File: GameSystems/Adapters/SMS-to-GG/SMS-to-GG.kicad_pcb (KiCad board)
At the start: 4 copper layers, 90.6 x 50.4 mm, 5 parts, among them J1 Master System Fingers, J2 Game Gear Slot

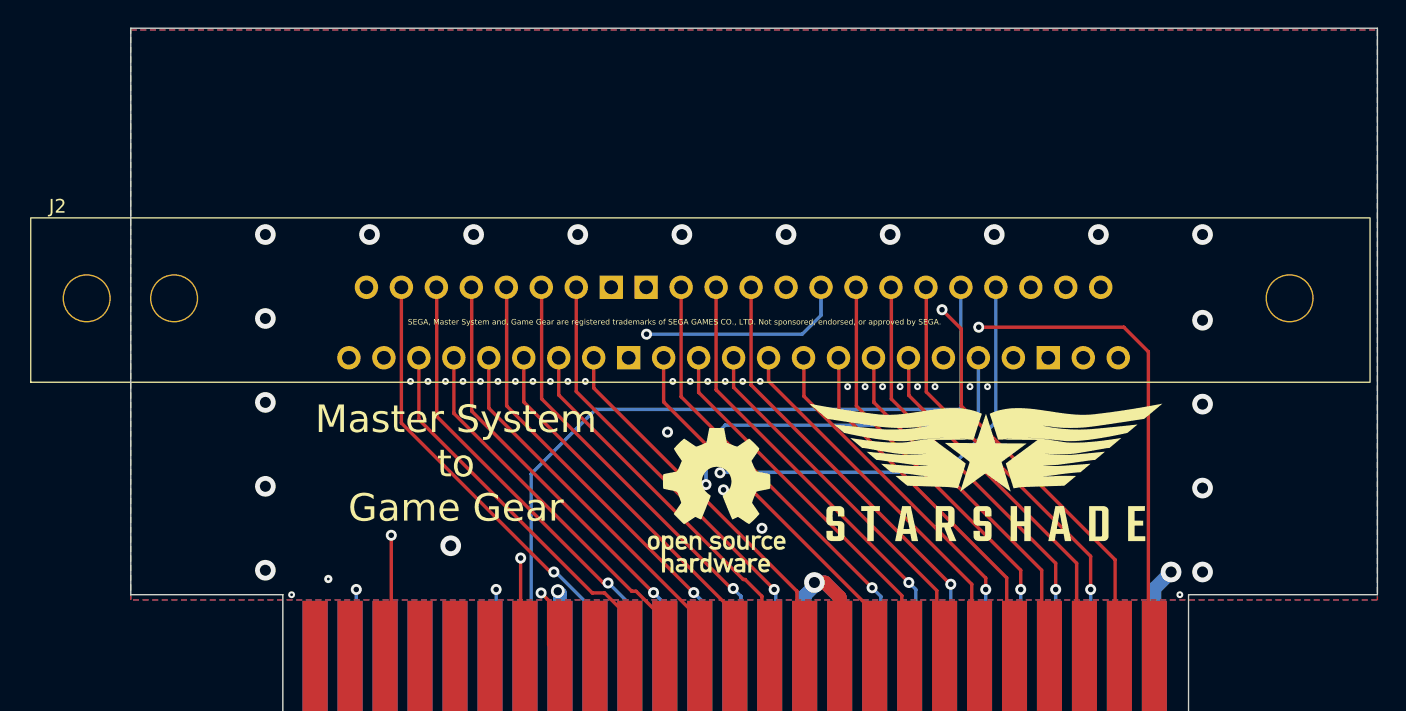
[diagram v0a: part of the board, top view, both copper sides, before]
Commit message: Update SMS to GG adapter and GG slot.
Was electrically correct but the NPTHs were slightly off.
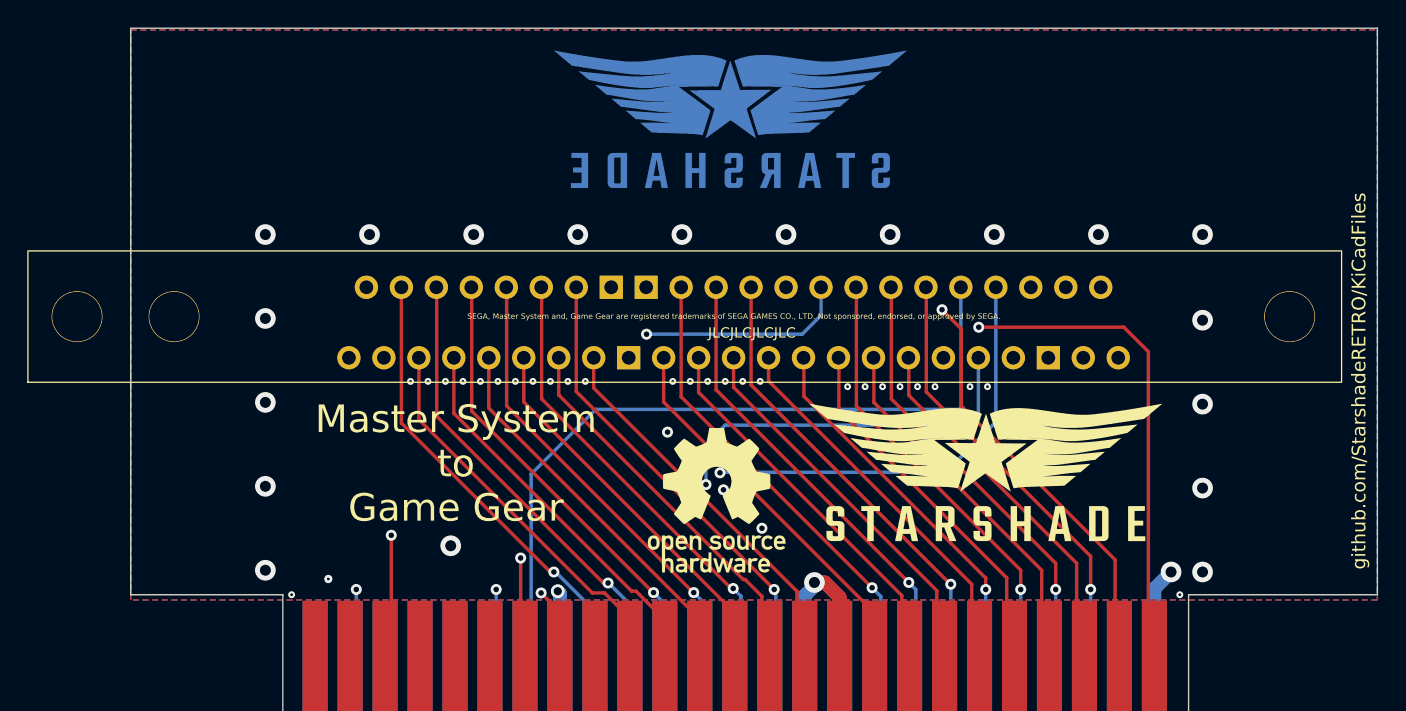
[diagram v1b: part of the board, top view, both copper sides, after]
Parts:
- G***: footprint !MiscFootprints:StarshadeLogoSmall -> !MiscFootprints:StarshadeLogoSmallMask
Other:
- board text added: "JLCJLCJLCJLC"
- board text added: "REV 2"
- board text added: "store.starshade.dev"
- board text removed: "REV 1"

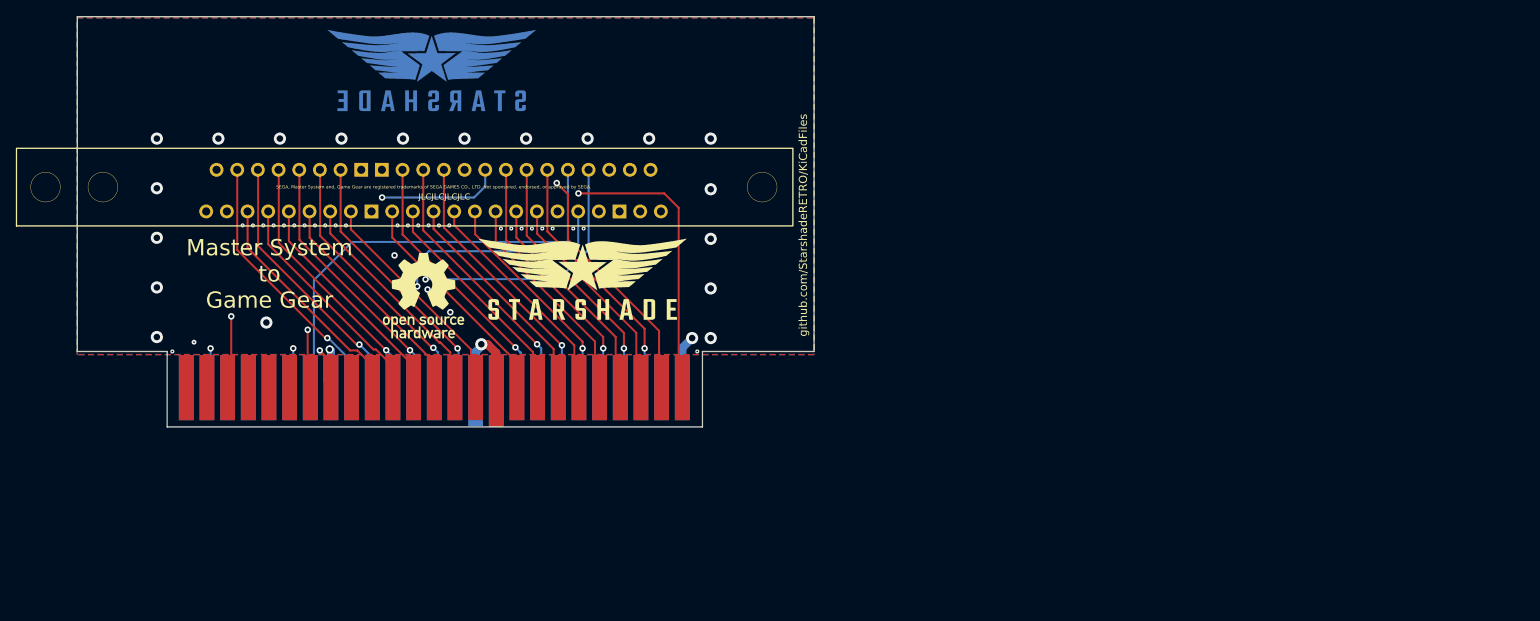
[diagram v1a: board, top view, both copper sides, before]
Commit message: SMS-to-GG revisions + more
* Updated the SMS-to-GG adapter from Rev 2 to Rev 4.
  * Rev 3 (not in repository):
    * Moved GG slot footprint up to allow room for the RetroSix GG slot connector PCB.
    * Added RetroSix GG slot FPC header directly to PCB.
  * Rev 4:
    * Fixed silkscreen disclaimers to refer to SEGA (Japan).
    * Moved JLCPCB "Specify Location" text to under the FPC header.
    * Made some general cosmetic improvements.
    * Updated project files to Latest KiCad version.
* Reorganized the libraries a little.
* Added 2-hole version of the Game Gear slot.
* Updated `.gitignore` for new KiCad version and some plugins.
* Updated the disclaimers in the `README.md` files.
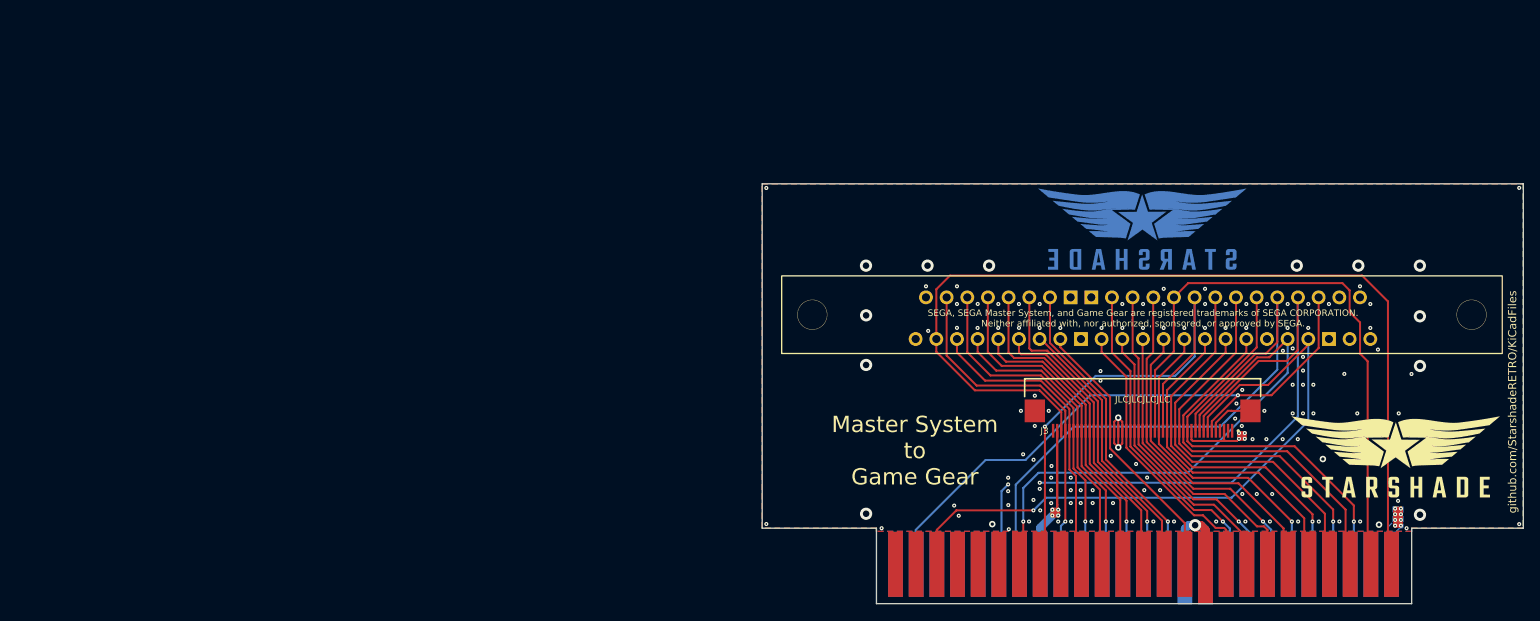
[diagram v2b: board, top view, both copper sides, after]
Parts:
- added J3: Gameslot GG Connector, !MiscFootprints:FPC Connector - 45-pin - Multiple, F.Cu at (150.6, 117.6)
- G***: footprint !MiscFootprints:StarshadeLogoSmall -> !MiscFootprints:Graphic - Starshade Logo - Silk - Small
- G***: footprint !MiscFootprints:OSHW -> !MiscFootprints:Graphic - OSHW Logo - Silk - Small; moved to B.Cu
- G***: footprint !MiscFootprints:StarshadeLogoSmallMask -> !MiscFootprints:Graphic - Starshade Logo - Mask - Small
- J1: value Master System Fingers -> SMS Fingers
- J2: footprint !SGFootprints:SG_GG_CARTRIDGE_SLOT -> !SGFootprints:SG_GG_CARTRIDGE_SLOT_2H
- moved G*** 102.3 mm to (181.7, 120.8)
- moved G*** 91.0 mm to (150.6, 122.7), turned to 180 degrees
- moved J1 89.8 mm to (150.7, 134.0)
- moved G*** 89.5 mm to (150.6, 92.8)
- moved J2 88.6 mm to (150.6, 103.7)
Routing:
- net +5V: track 11.4 -> 51.1 mm, vias 2 -> 16
- net Write: track 79.8 -> 118.4 mm, vias 1 -> 0
- net Read: track 42.5 -> 74.8 mm, vias 1 -> 0
- net Refresh: track 58.5 -> 87.2 mm
- net M1: track 55.4 -> 79.0 mm
- net A15: track 42.4 -> 64.4 mm, vias 2 -> 1
- net Reset: track 62.5 -> 84.0 mm
- net M8-B: track 31.9 -> 52.4 mm
- net A14: track 27.0 -> 46.2 mm
- net A13: track 31.9 -> 50.1 mm
- net IO_Request: track 50.7 -> 68.7 mm, vias 2 -> 1
- net A8: track 27.0 -> 43.9 mm
- net GND: track 19.9 -> 36.3 mm, vias 51 -> 140
- net A9: track 31.9 -> 47.7 mm
- net A11: track 27.0 -> 41.6 mm
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- added copper zone on B.Cu, net +5V
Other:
- board size 90.6 x 50.4 mm -> 93.5 x 51.6 mm
- board text added: "0.1000 mm / 0.1000 mm"
- board text added: "0.2000 mm"
- board text added: "1.6167 mm"
- board text added: "4"
- board text added: "93.5460 mm x 51.5940 mm"
- board text added: "BOARD CHARACTERISTICS"
- board text added: "Board Thickness:"
- board text added: "Board overall dimensions:"
- board text added: "Castellated pads:"
- board text added: "Copper Finish:"
- board text added: "Copper Layer Count:"
- board text added: "ENIG"
- board text added: "Edge card connectors:"
- board text added: "Impedance Control:"
- board text added: "Min hole diameter:"
- board text added: "Min track/spacing:"
- board text added: "No"
- board text added: "Plated Board Edge:"
- board text added: "REV ${REVISION}"
- board text added: "SEGA, SEGA Master System, and Game Gear are registered trademarks of SEGA CORPORATION. Neither affiliated with, nor authorized, sponsored, or approved by SEGA."
- board text added: "Yes, Bevelled"
- board text removed: "REV 2"
- board text removed: "SEGA, Master System and, Game Gear are registered trademarks of SEGA GAMES CO., LTD. Not sponsored, endorsed, or approved by SEGA."
